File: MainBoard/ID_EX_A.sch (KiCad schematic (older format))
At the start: 4 parts, among them U63 74AHCT574, U64 74AHCT574

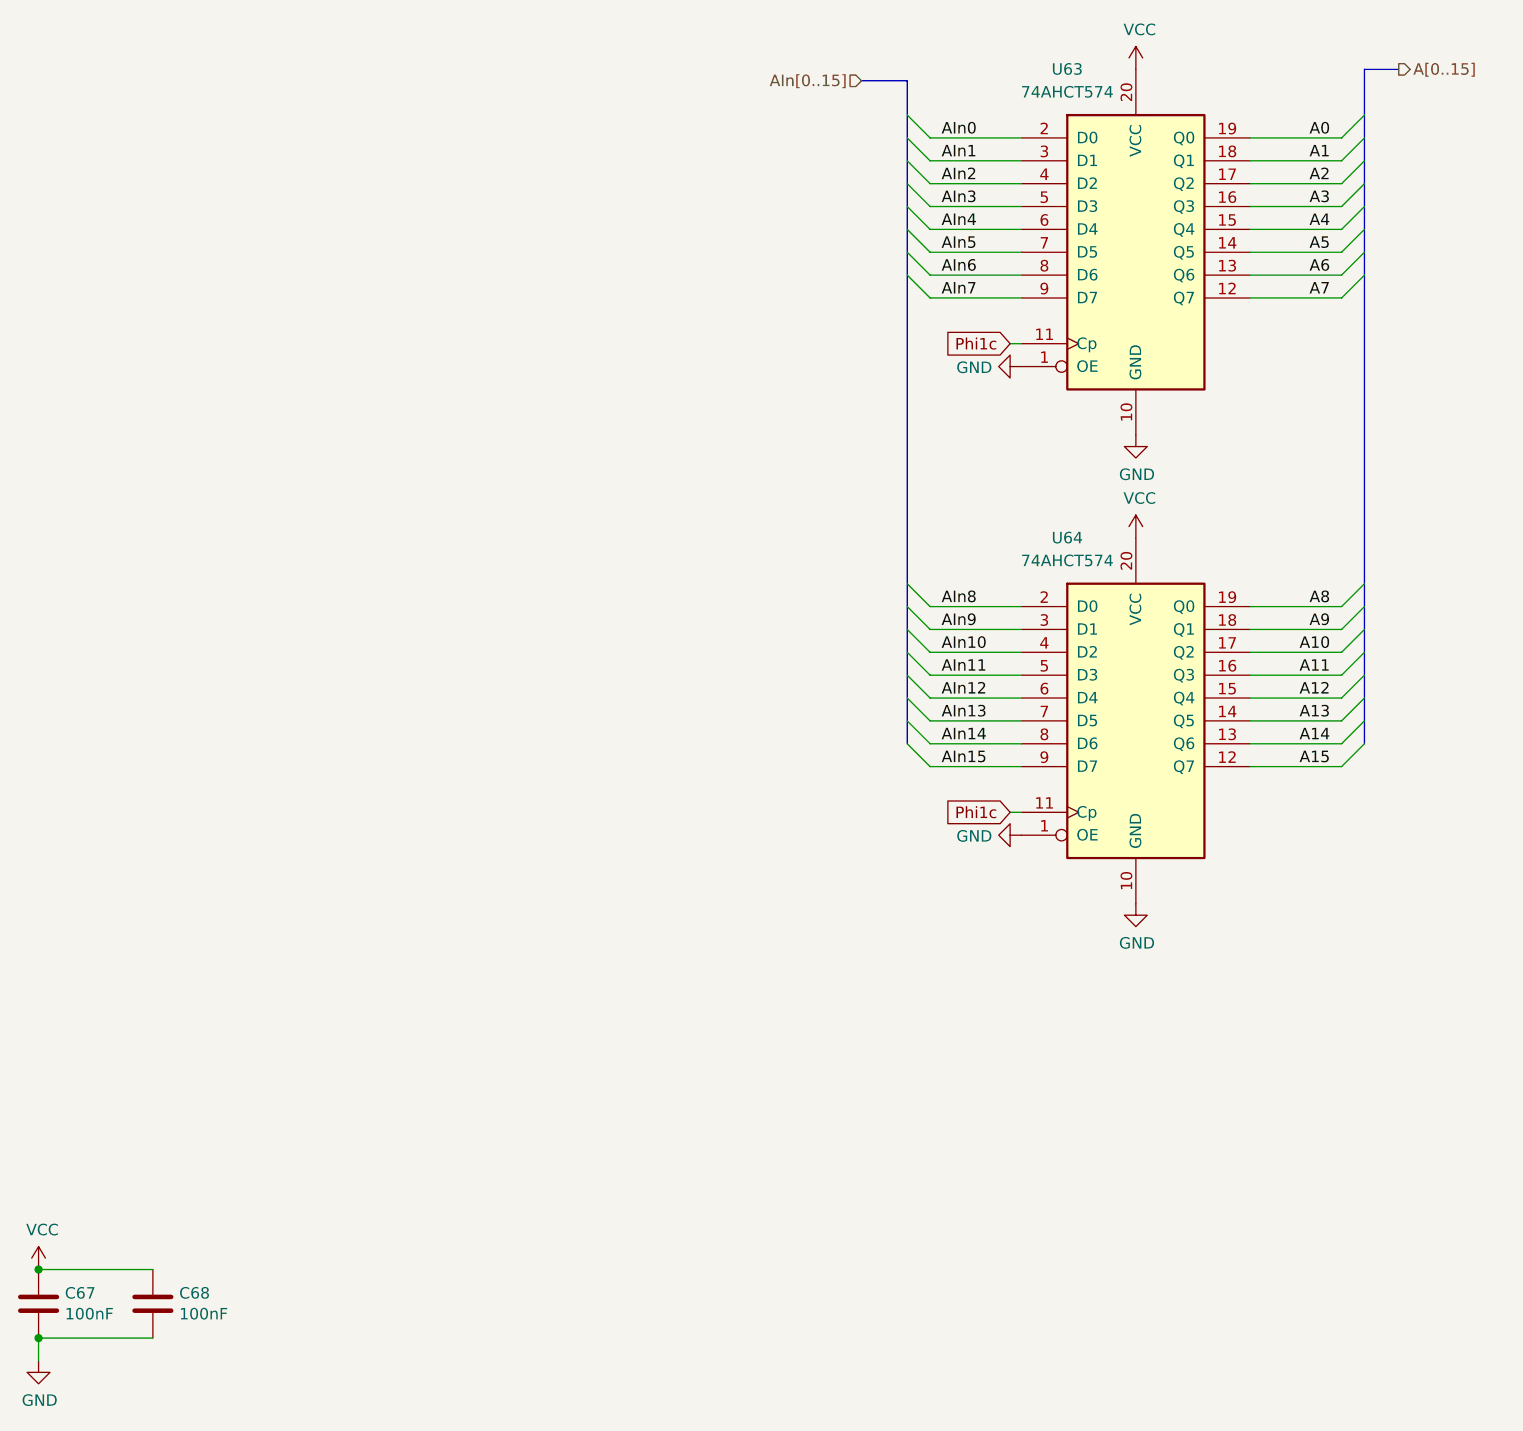
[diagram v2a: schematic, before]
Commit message: Replace 74AHCT574 with 74ABT16374
This greatly reduces the number of components on the PCB and the amount
of board space needed for the CPU.
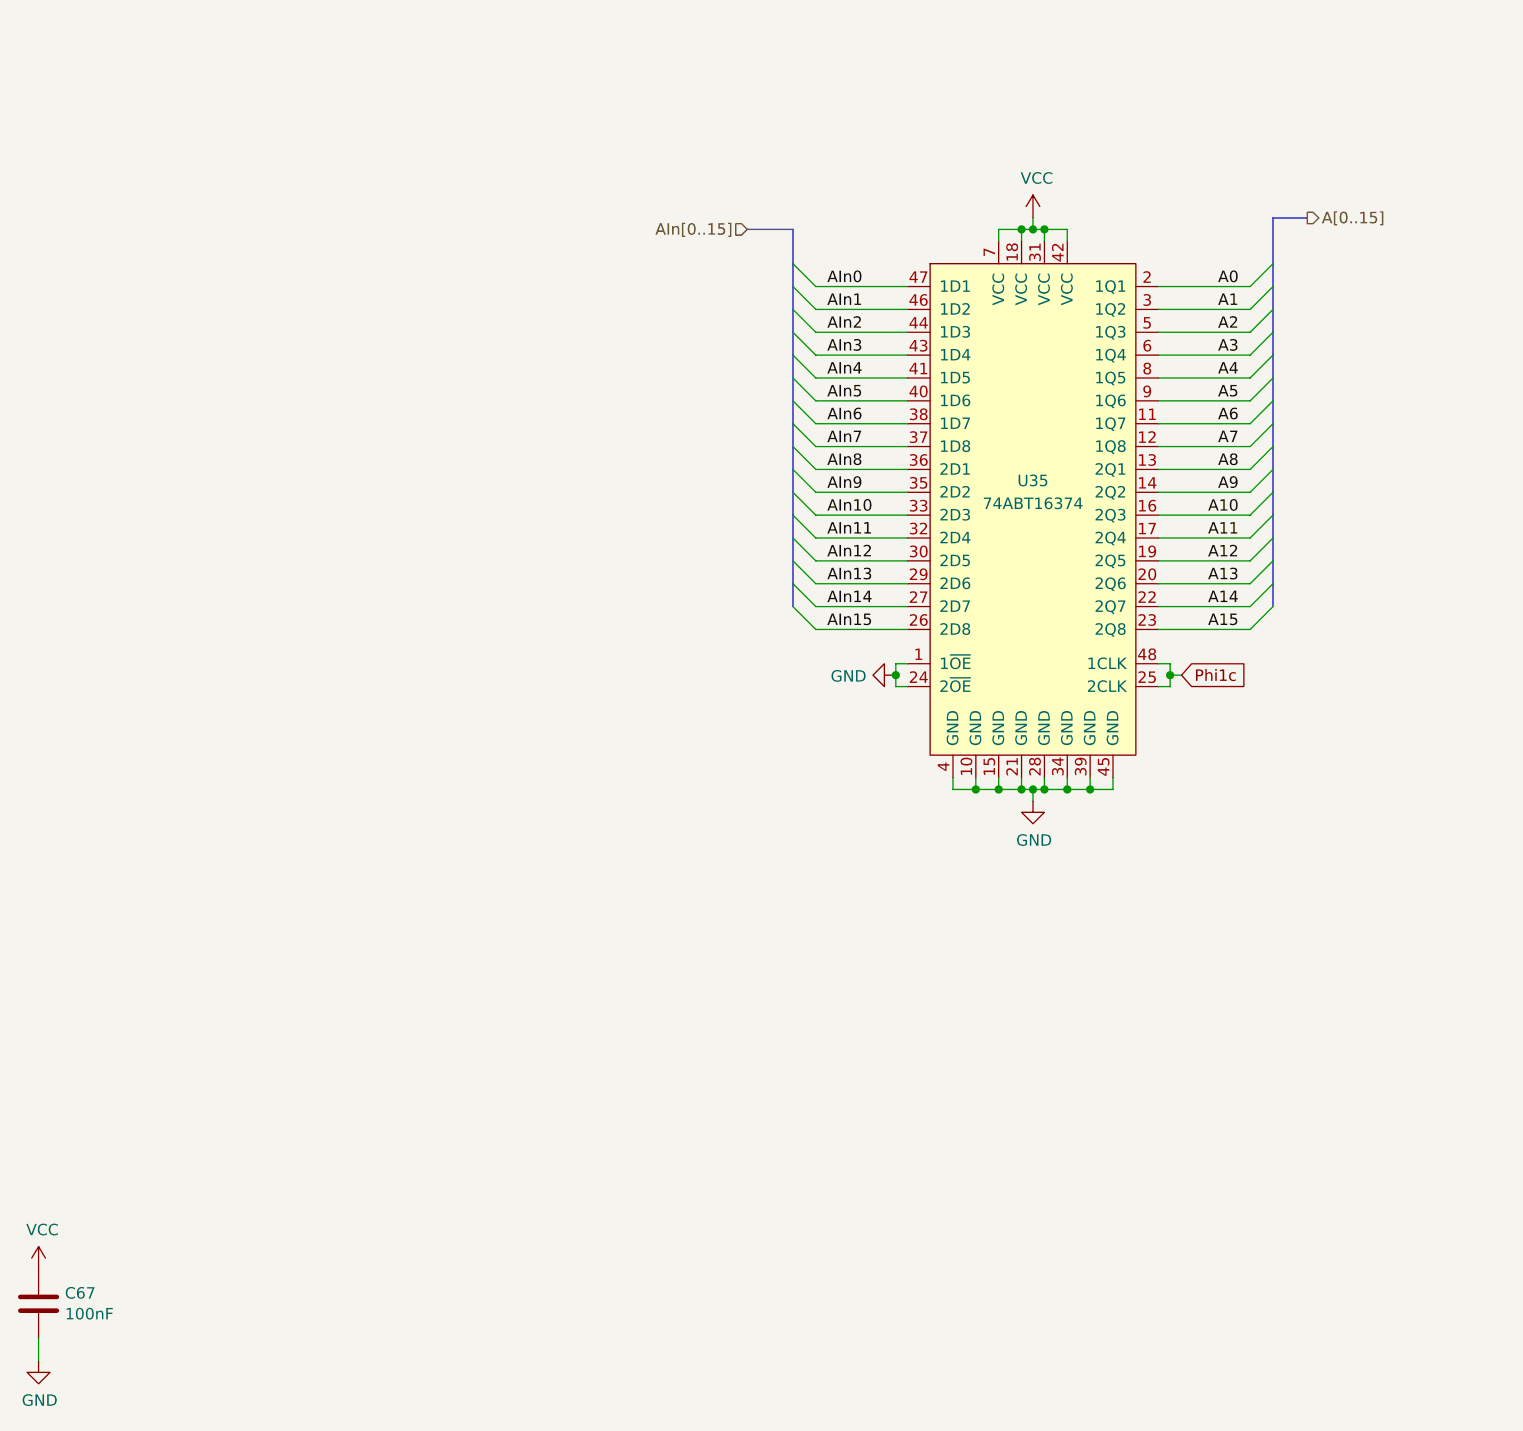
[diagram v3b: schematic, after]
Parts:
- removed C68: 100nF, Capacitor_SMD:C_0603_1608Metric_Pad1.08x0.95mm_HandSolder, symbol Device:C
- removed U63, U64: 74AHCT574, Package_SO:TSSOP-20_4.4x6.5mm_P0.65mm, symbol 74xx:74LS574
- added U35: 74ABT16374, Package_SO:TSSOP-48_8x12.5mm_P0.5mm, symbol 74xx:74ABT16374
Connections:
- net A0: now also U35.2 (1Q1)
- net A1: now also U35.3 (1Q2)
- net A10: now also U35.16 (2Q3)
- net A11: now also U35.17 (2Q4)
- net A12: now also U35.19 (2Q5)
- net A13: now also U35.20 (2Q6)
- net A14: now also U35.22 (2Q7)
- net A15: now also U35.23 (2Q8)
- net A2: now also U35.5 (1Q3)
- net A3: now also U35.6 (1Q4)
- net A4: now also U35.8 (1Q5)
- net A5: now also U35.9 (1Q6)
- net A6: now also U35.11 (1Q7)
- net A7: now also U35.12 (1Q8)
- net A8: now also U35.13 (2Q1)
- net A9: now also U35.14 (2Q2)
- net AIn0: now also U35.47 (1D1)
- net AIn1: now also U35.46 (1D2)
- net AIn10: now also U35.33 (2D3)
- net AIn11: now also U35.32 (2D4)
- net AIn12: now also U35.30 (2D5)
- net AIn13: now also U35.29 (2D6)
- net AIn14: now also U35.27 (2D7)
- net AIn15: now also U35.26 (2D8)
- net AIn2: now also U35.44 (1D3)
- net AIn3: now also U35.43 (1D4)
- net AIn4: now also U35.41 (1D5)
- net AIn5: now also U35.40 (1D6)
- net AIn6: now also U35.38 (1D7)
- net AIn7: now also U35.37 (1D8)
- net AIn8: now also U35.36 (2D1)
- net AIn9: now also U35.35 (2D2)
- net GND: now also U35.1 (1~OE), U35.10 (GND), U35.15 (GND), U35.21 (GND), U35.24 (2~OE), U35.28 (GND), U35.34 (GND), U35.39 (GND), U35.4 (GND), U35.45 (GND)
- net Phi1c: now also U35.25 (2CLK), U35.48 (1CLK)
- net VCC: now also U35.18 (VCC), U35.31 (VCC), U35.42 (VCC), U35.7 (VCC)

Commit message: Add hazard control logic to ID.
TODO: The simulator has not been updated.
TODO: Hardware for operand forwarding has not been added yet.
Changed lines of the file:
@@
 $Descr USLetter 11000 8500
 encoding utf-8
-Sheet 30 35
+Sheet 30 36
 Title ""
 Date "2021-04-01"
@@
 AR Path="/5FED3839/5FD8C8F4/6082B7A1" Ref="#PWR?"  Part="1"
 AR Path="/5FED3839/5FE081C3/6082B7A1" Ref="#PWR0262"  Part="1"
-F 0 "#PWR0262" H 4600 4200 50  0001 C CNN
+AR Path="/5FED3839/60693BE9/6082B7A1" Ref="#PWR0373"  Part="1"
+F 0 "#PWR0373" H 4600 4200 50  0001 C CNN
 F 1 "GND" V 4605 4322 50  0000 R CNN
 F 2 "" H 4600 4450 50  0001 C CNN
@@
 AR Path="/5FE35007/5FD0D8DC/5FD4714C/6082B7A8" Ref="#PWR?"  Part="1"
 AR Path="/5FED3839/5FE081C3/6082B7A8" Ref="#PWR0263"  Part="1"
-F 0 "#PWR0263" H 5200 2300 50  0001 C CNN
+AR Path="/5FED3839/60693BE9/6082B7A8" Ref="#PWR0374"  Part="1"
+F 0 "#PWR0374" H 5200 2300 50  0001 C CNN
 F 1 "VCC" H 5217 2623 50  0000 C CNN
 F 2 "" H 5200 2450 50  0001 C CNN
@@
 AR Path="/5FE35007/5FD0D8DC/5FD4714C/6082B7AE" Ref="#PWR?"  Part="1"
 AR Path="/5FED3839/5FE081C3/6082B7AE" Ref="#PWR0264"  Part="1"
-F 0 "#PWR0264" H 5200 4750 50  0001 C CNN
+AR Path="/5FED3839/60693BE9/6082B7AE" Ref="#PWR0375"  Part="1"
+F 0 "#PWR0375" H 5200 4750 50  0001 C CNN
 F 1 "GND" H 5205 4827 50  0000 C CNN
 F 2 "" H 5200 5000 50  0001 C CNN
@@
 AR Path="/5FE35007/5FCE2082/6082B7D9" Ref="U?"  Part="1"
 AR Path="/5FED3839/5FE081C3/6082B7D9" Ref="U35"  Part="1"
-F 0 "U35" H 5200 3600 50  0000 C CNN
+AR Path="/5FED3839/60693BE9/6082B7D9" Ref="U42"  Part="1"
+F 0 "U42" H 5200 3600 50  0000 C CNN
 F 1 "74ABT16374" H 5200 3500 50  0000 C CNN
 F 2 "Package_SO:TSSOP-48_8x12.5mm_P0.5mm" H 5250 3400 50  0001 C CNN
@@
 	4600 4500 4650 4500
 Connection ~ 4600 4450
-Wire Bus Line
-	6250 2450 6250 4150
-Wire Bus Line
-	4150 2500 4150 4150
 Wire Wire Line
 	850  7450 850  7350
@@
 AR Path="/5FED3839/5FD8C8F4/5FE19A90" Ref="#PWR?"  Part="1"
 AR Path="/5FED3839/5FE081C3/5FE19A90" Ref="#PWR0425"  Part="1"
-F 0 "#PWR0425" H 850 7200 50  0001 C CNN
+AR Path="/5FED3839/60693BE9/5FE19A90" Ref="#PWR0376"  Part="1"
+F 0 "#PWR0376" H 850 7200 50  0001 C CNN
 F 1 "GND" H 855 7277 50  0000 C CNN
 F 2 "" H 850 7450 50  0001 C CNN
@@
 AR Path="/5FED3839/5FD8C8F4/5FE19A8A" Ref="#PWR?"  Part="1"
 AR Path="/5FED3839/5FE081C3/5FE19A8A" Ref="#PWR0424"  Part="1"
-F 0 "#PWR0424" H 850 6900 50  0001 C CNN
+AR Path="/5FED3839/60693BE9/5FE19A8A" Ref="#PWR0377"  Part="1"
+F 0 "#PWR0377" H 850 6900 50  0001 C CNN
 F 1 "VCC" H 867 7223 50  0000 C CNN
 F 2 "" H 850 7050 50  0001 C CNN
@@
 AR Path="/5FED3839/5FD8C8F4/5FE19A84" Ref="C?"  Part="1"
 AR Path="/5FED3839/5FE081C3/5FE19A84" Ref="C67"  Part="1"
-F 0 "C67" H 965 7246 50  0000 L CNN
+AR Path="/5FED3839/60693BE9/5FE19A84" Ref="C30"  Part="1"
+F 0 "C30" H 965 7246 50  0000 L CNN
 F 1 "100nF" H 965 7155 50  0000 L CNN
 F 2 "Capacitor_SMD:C_0603_1608Metric_Pad1.08x0.95mm_HandSolder" H 888 7050 50  0001 C CNN
@@
 	1    0    0    -1
 $EndComp
+Wire Bus Line
+	4150 2500 4150 4150
+Wire Bus Line
+	6250 2450 6250 4150
 $EndSCHEMATC

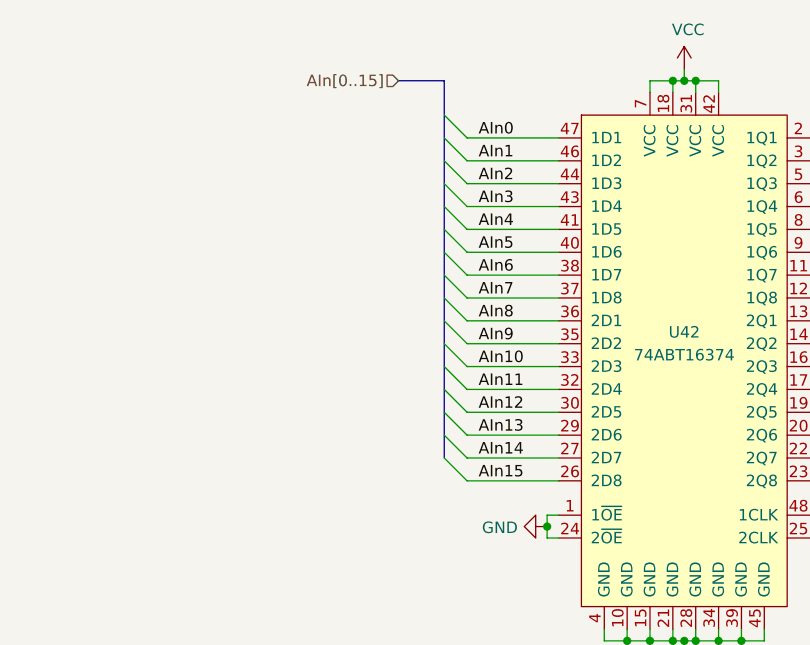
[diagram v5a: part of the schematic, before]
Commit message: Add hardware for operand forwarding, and place on the PCB.
Resolve RAW hazards by forwarding results from a subsequent pipeline stage.

TODO: The simulator has not been updated yet.
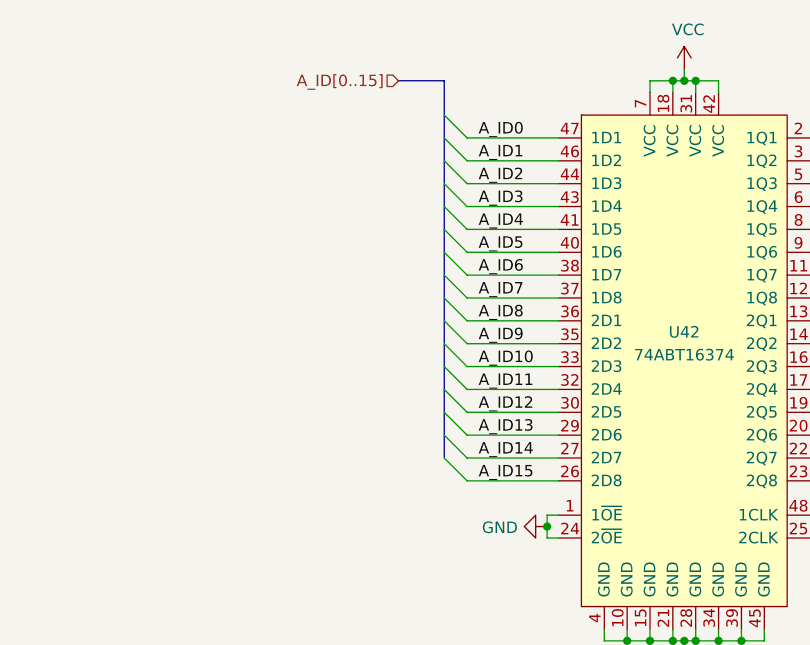
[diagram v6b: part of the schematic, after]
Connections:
- net AIn0 renamed A_ID0
- net AIn1 renamed A_ID1
- net AIn10 renamed A_ID10
- net AIn11 renamed A_ID11
- net AIn12 renamed A_ID12
- net AIn13 renamed A_ID13
- net AIn14 renamed A_ID14
- net AIn15 renamed A_ID15
- net AIn2 renamed A_ID2
- net AIn3 renamed A_ID3
- net AIn4 renamed A_ID4
- net AIn5 renamed A_ID5
- net AIn6 renamed A_ID6
- net AIn7 renamed A_ID7
- net AIn8 renamed A_ID8
- net AIn9 renamed A_ID9
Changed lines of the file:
@@
 $Descr USLetter 11000 8500
 encoding utf-8
-Sheet 30 36
+Sheet 30 38
 Title ""
 Date "2021-04-01"
@@
 	4150 2750 4250 2850
 Text Label 4300 2750 0    50   ~ 0
-AIn0
+A_ID0
 Wire Wire Line
 	4250 2750 4650 2750
@@
 	6250 3450 6150 3550
 Text Label 4300 2850 0    50   ~ 0
-AIn1
+A_ID1
 Text Label 4300 2950 0    50   ~ 0
-AIn2
+A_ID2
 Text Label 4300 3050 0    50   ~ 0
-AIn3
+A_ID3
 Text Label 4300 3150 0    50   ~ 0
-AIn4
+A_ID4
 Text Label 4300 3250 0    50   ~ 0
-AIn5
+A_ID5
 Text Label 4300 3350 0    50   ~ 0
-AIn6
+A_ID6
 Text Label 4300 3450 0    50   ~ 0
-AIn7
+A_ID7
 Text Label 4300 3550 0    50   ~ 0
-AIn8
+A_ID8
 Text Label 4300 3650 0    50   ~ 0
-AIn9
+A_ID9
 Text Label 4300 3750 0    50   ~ 0
-AIn10
+A_ID10
 Wire Wire Line
 	6150 3650 5750 3650
@@
 A10
 Text HLabel 3950 2500 0    50   Input ~ 0
-AIn[0..15]
+A_ID[0..15]
 Text HLabel 6400 2450 2    50   Output ~ 0
 A[0..15]
@@
 	4150 3750 4250 3850
 Text Label 4300 3850 0    50   ~ 0
-AIn11
+A_ID11
 Text Label 4300 3950 0    50   ~ 0
-AIn12
+A_ID12
 Text Label 4300 4050 0    50   ~ 0
-AIn13
+A_ID13
 Wire Wire Line
 	4250 4250 4650 4250
@@
 	4150 4050 4250 4150
 Text Label 4300 4150 0    50   ~ 0
-AIn14
+A_ID14
 Text Label 4300 4250 0    50   ~ 0
-AIn15
+A_ID15
 Wire Wire Line
 	6150 4050 5750 4050
